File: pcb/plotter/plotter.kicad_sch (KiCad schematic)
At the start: 58 parts, among them J1 SH 1106 Display, J10 Limit switches, J2 SWD, J3 Console, J4 Micro_SD_Card_Det, J5 USB_B_Micro, SW1 Rotary_Encoder_Switch, U1 STM32F405RGTx, U4 PUSB3F96, U6 AP1117-33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

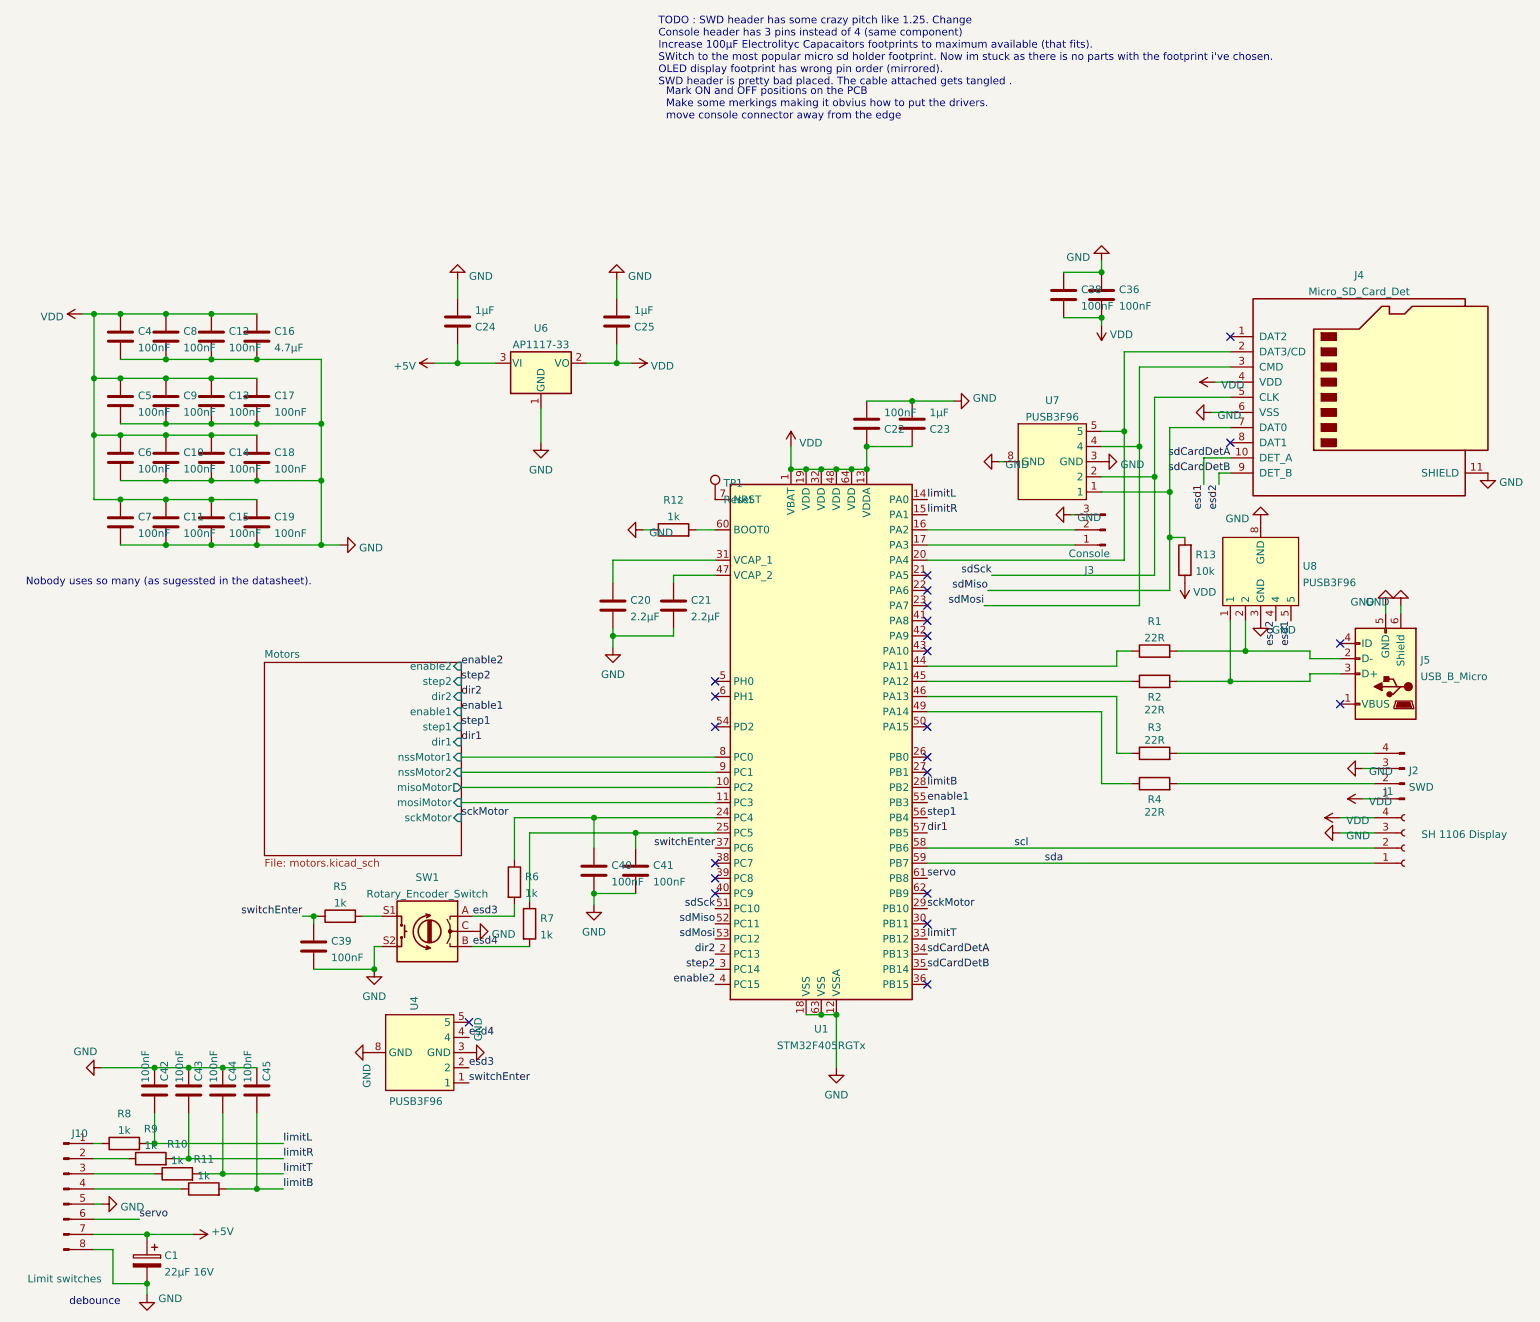
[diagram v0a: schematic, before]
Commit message: Steppers config upudated
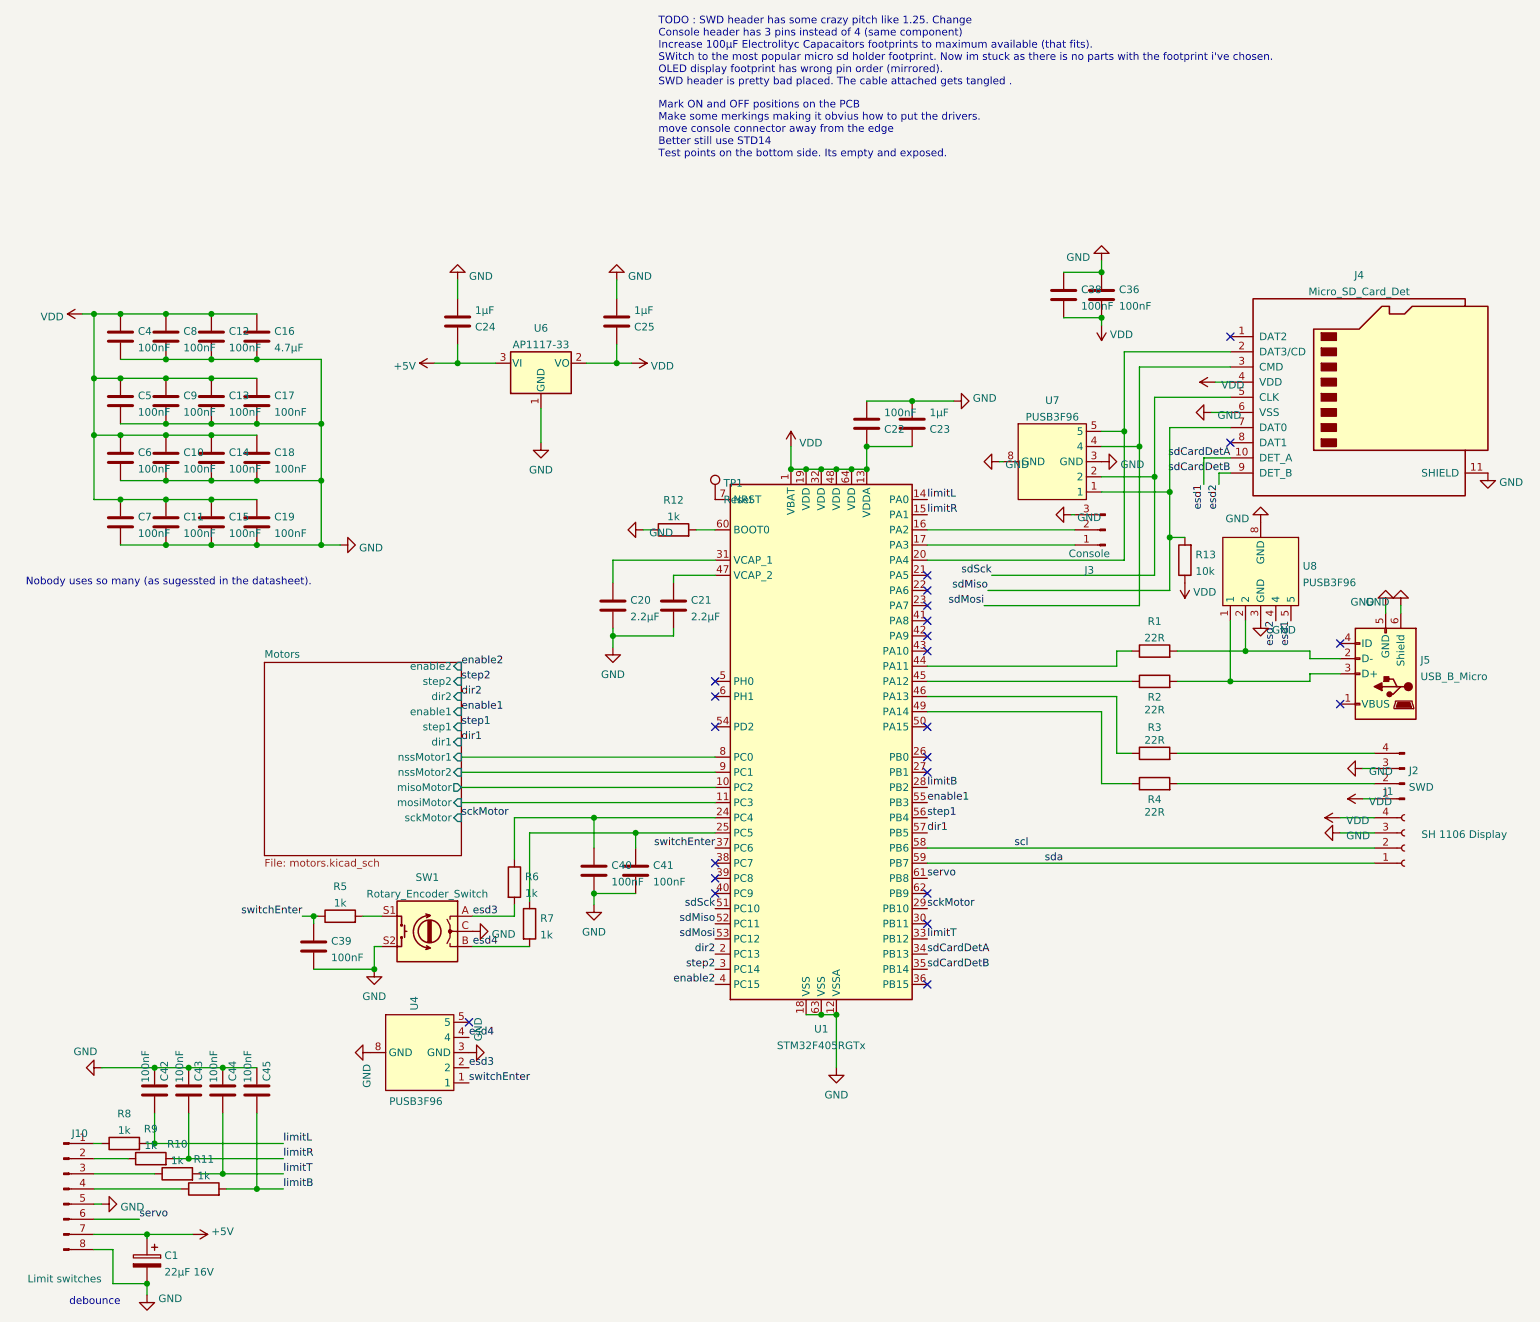
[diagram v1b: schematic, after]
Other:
- note added: "Mark ON and OFF positions on the PCB Make some merkings making it obvius how to put the drivers. move console connector away from the edge Better still use STD14 Test points on the bottom side. Its empty and exposed."
- note removed: "Mark ON and OFF positions on the PCB Make some merkings making it obvius how to put the drivers. move console connector away from the edge"
